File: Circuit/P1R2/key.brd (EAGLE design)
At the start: 160 x 100 mm, 8 parts, among them J1 1981584-1, U3 MINI54TAN

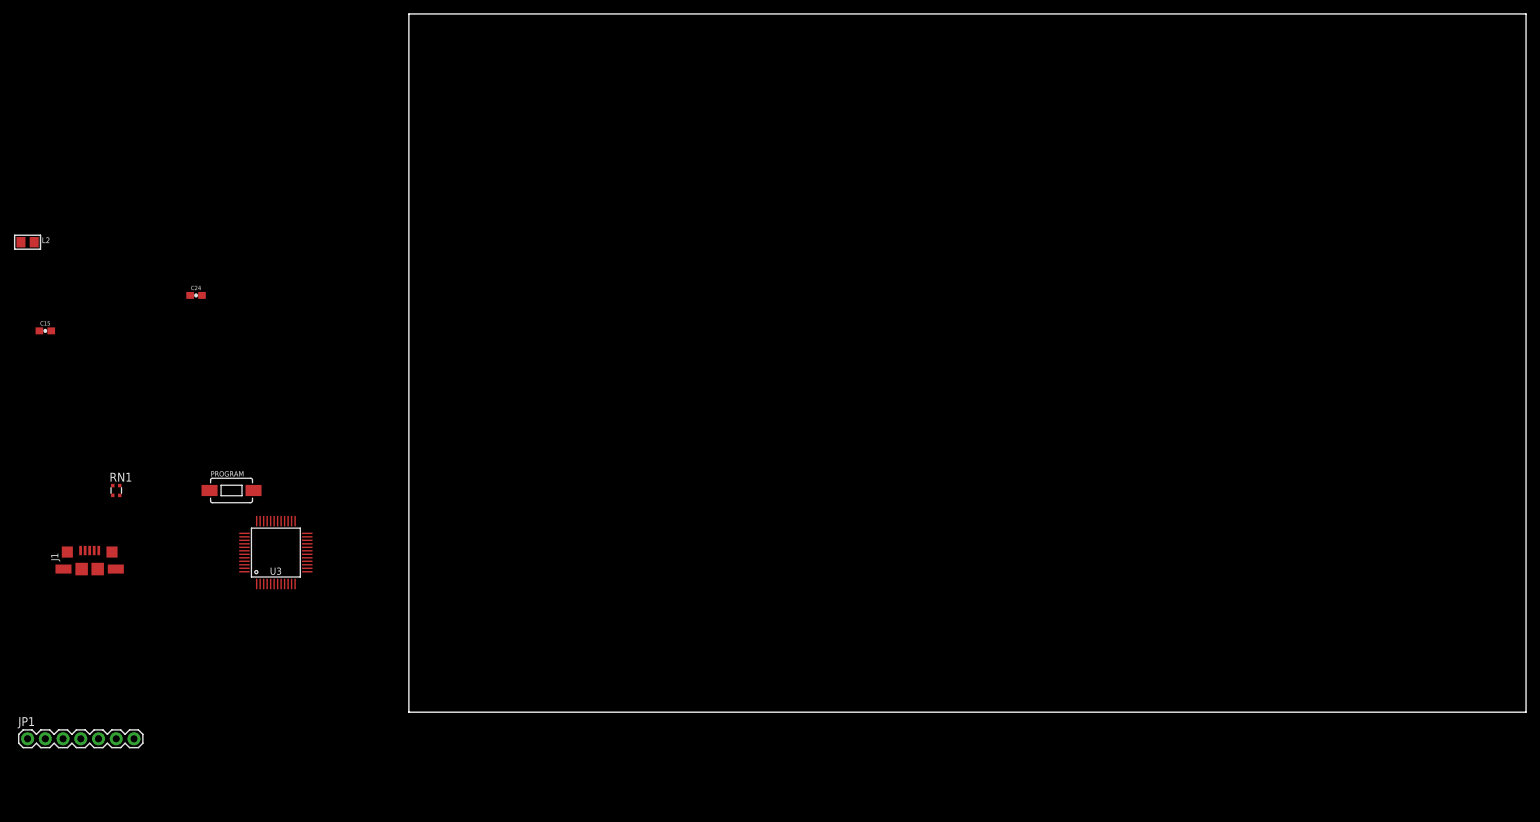
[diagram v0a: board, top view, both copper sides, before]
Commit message: Preliminary key completed
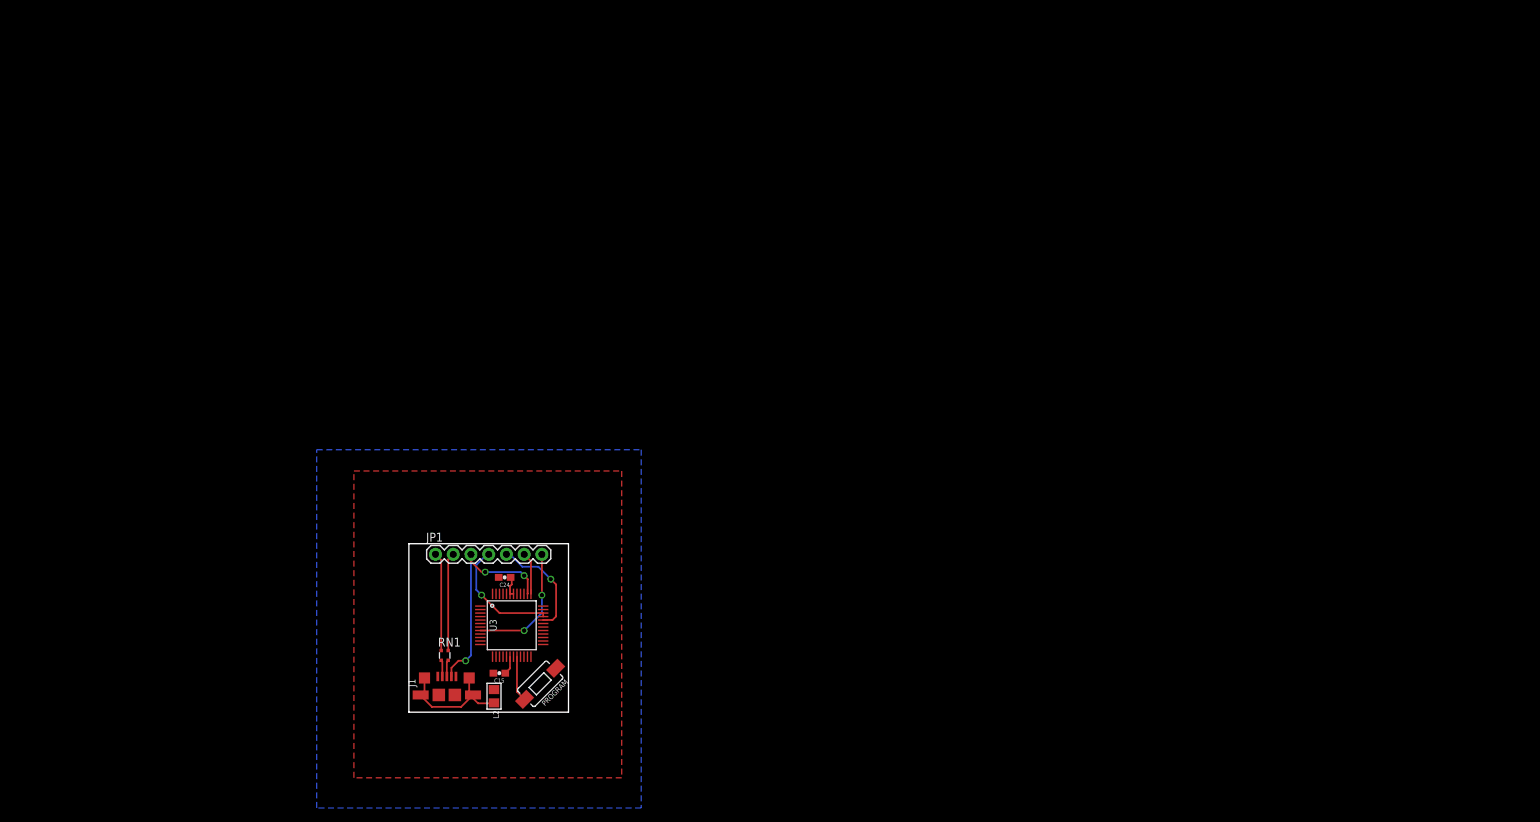
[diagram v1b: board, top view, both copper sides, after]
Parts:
- moved L2 93.2 mm to (12.2, 2.29), turned to 270 degrees
- moved C15 81.4 mm to (13.0, 5.59), turned to 180 degrees
- moved JP1 64.1 mm to (3.81, 22.6)
- moved C24 59.9 mm to (13.7, 19.3), turned to 180 degrees
- moved J1 54.2 mm to (5.44, 1.02)
- moved RN1 52.6 mm to (5.13, 8.13)
- moved PROGRAM 52.2 mm to (18.8, 4.06), turned to 225 degrees
- moved U3 35.4 mm to (14.7, 12.4), turned to 270 degrees
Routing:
- net ID: track 0.00 -> 32.3 mm, vias 0 -> 3
- net USB_SHIELD: track 0.00 -> 18.8 mm
- net RESET_B: track 0.00 -> 18.3 mm, vias 0 -> 2
- net SWD_DIO: track 0.00 -> 17.4 mm, vias 0 -> 1
- net SWD_CLK: track 0.00 -> 15.5 mm, vias 0 -> 1
- net USB_D_N: track 0.00 -> 14.1 mm
- net USB_D_P: track 0.00 -> 14.1 mm
- net N$17: track 0.00 -> 6.56 mm
- net P0.1: track 0.00 -> 6.06 mm
- net 3.3V: track 0.00 -> 3.03 mm
- net N$18: track 0.00 -> 2.64 mm
- net USB_CON_P: track 0.00 -> 2.39 mm
- net USB_CON_N: track 0.00 -> 2.38 mm
- added copper zone on layer 1, net GND
- added copper zone on layer 16, net GND
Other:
- board size 160 x 100 mm -> 22.9 x 24.1 mm

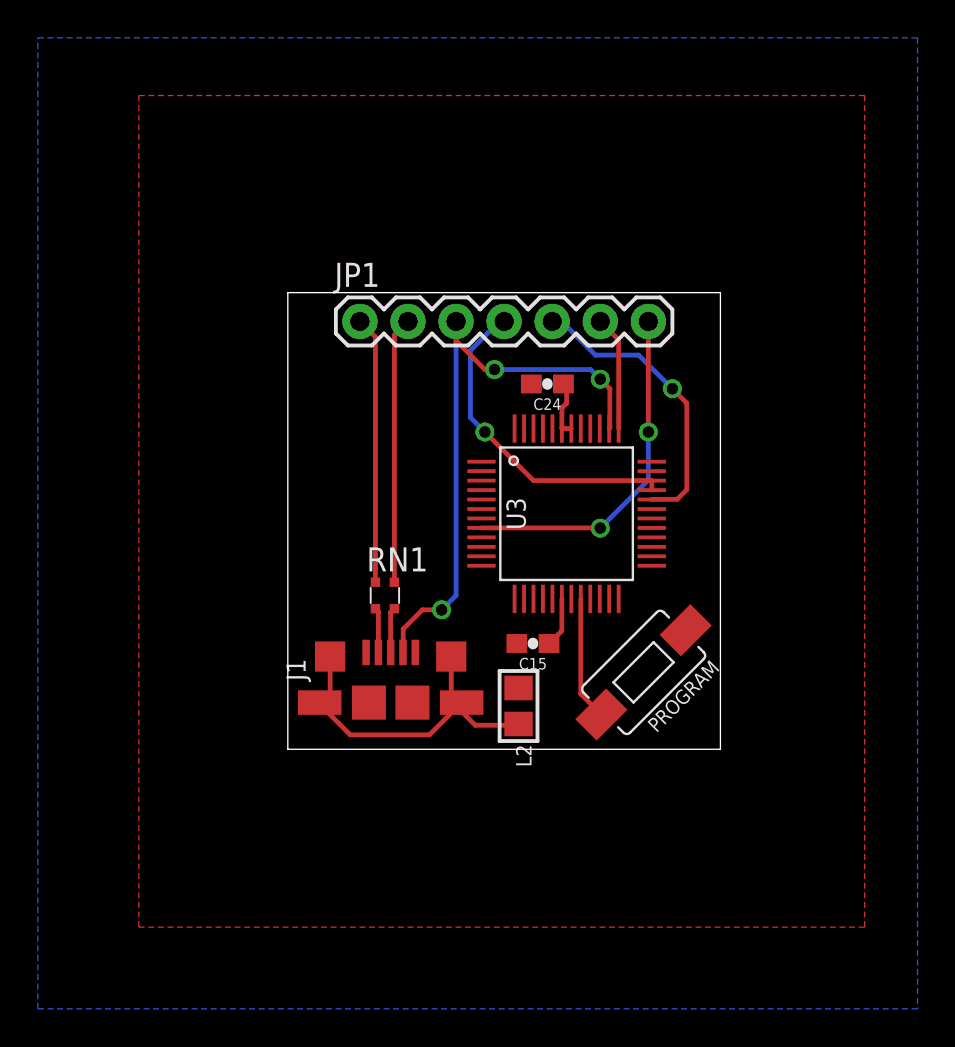
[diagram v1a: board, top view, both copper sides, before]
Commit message: Forum boards done
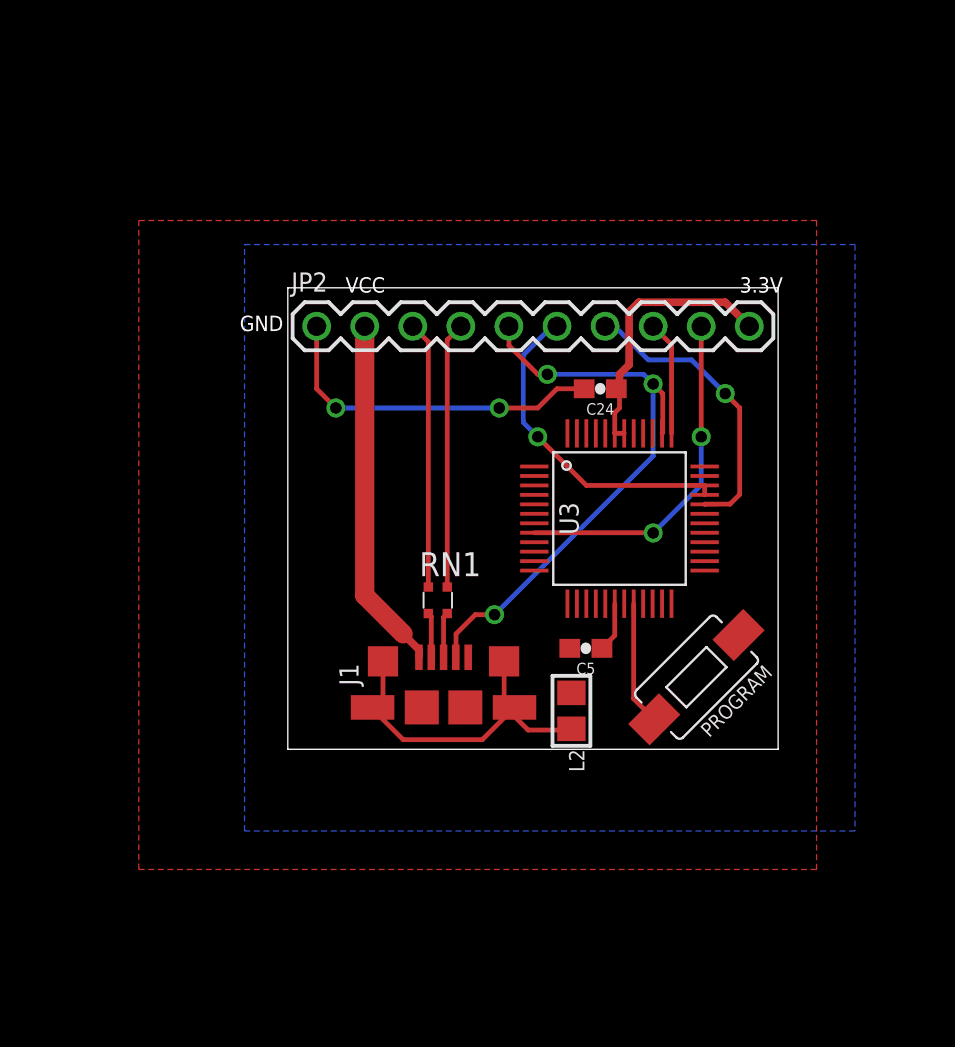
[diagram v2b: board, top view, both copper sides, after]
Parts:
- removed C15: 0.1uF, appfruits:0603-CAP
- removed JP1: (no value), SparkFun-Connectors:1X07
- added C5: 0.1uF, appfruits:0603-CAP
- added JP2: M100.1, umich:1X10
- moved C24 2.81 mm to (16.5, 19.1)
- moved L2 2.81 mm to (15.0, 2.03)
- moved PROGRAM 2.81 mm to (21.6, 3.81)
- moved RN1 2.81 mm to (7.92, 7.87)
- moved U3 2.81 mm to (17.5, 12.2)
- moved J1 2.81 mm to (8.23, 0.76)
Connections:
- net 3.3V: now also JP2.10
- net GND: now also C5.2, JP2.1; no longer C15.2
- net ID: now also JP2.5; no longer JP1.3
- net N$18: now also C5.1; no longer C15.1
- net P0.1: now also JP2.8; no longer JP1.6
- net RESET_B: now also JP2.9; no longer JP1.7
- net SWD_CLK: now also JP2.7; no longer JP1.5
- net SWD_DIO: now also JP2.6; no longer JP1.4
- net USB_D_N: now also JP2.3; no longer JP1.1
- net USB_D_P: now also JP2.4; no longer JP1.2
- net VCC: now also JP2.2
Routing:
- net VCC: track 0.00 -> 18.7 mm
- net GND: track 0.00 -> 18.3 mm, vias 0 -> 2
- net 3.3V: track 3.03 -> 14.6 mm
- net ID: track 32.3 -> 31.7 mm
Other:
- board size 22.9 x 24.1 mm -> 25.9 x 24.4 mm
- board text added: "3.3V"
- board text added: "GND"
- board text added: "VCC"
